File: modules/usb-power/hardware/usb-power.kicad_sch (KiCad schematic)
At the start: 0 parts

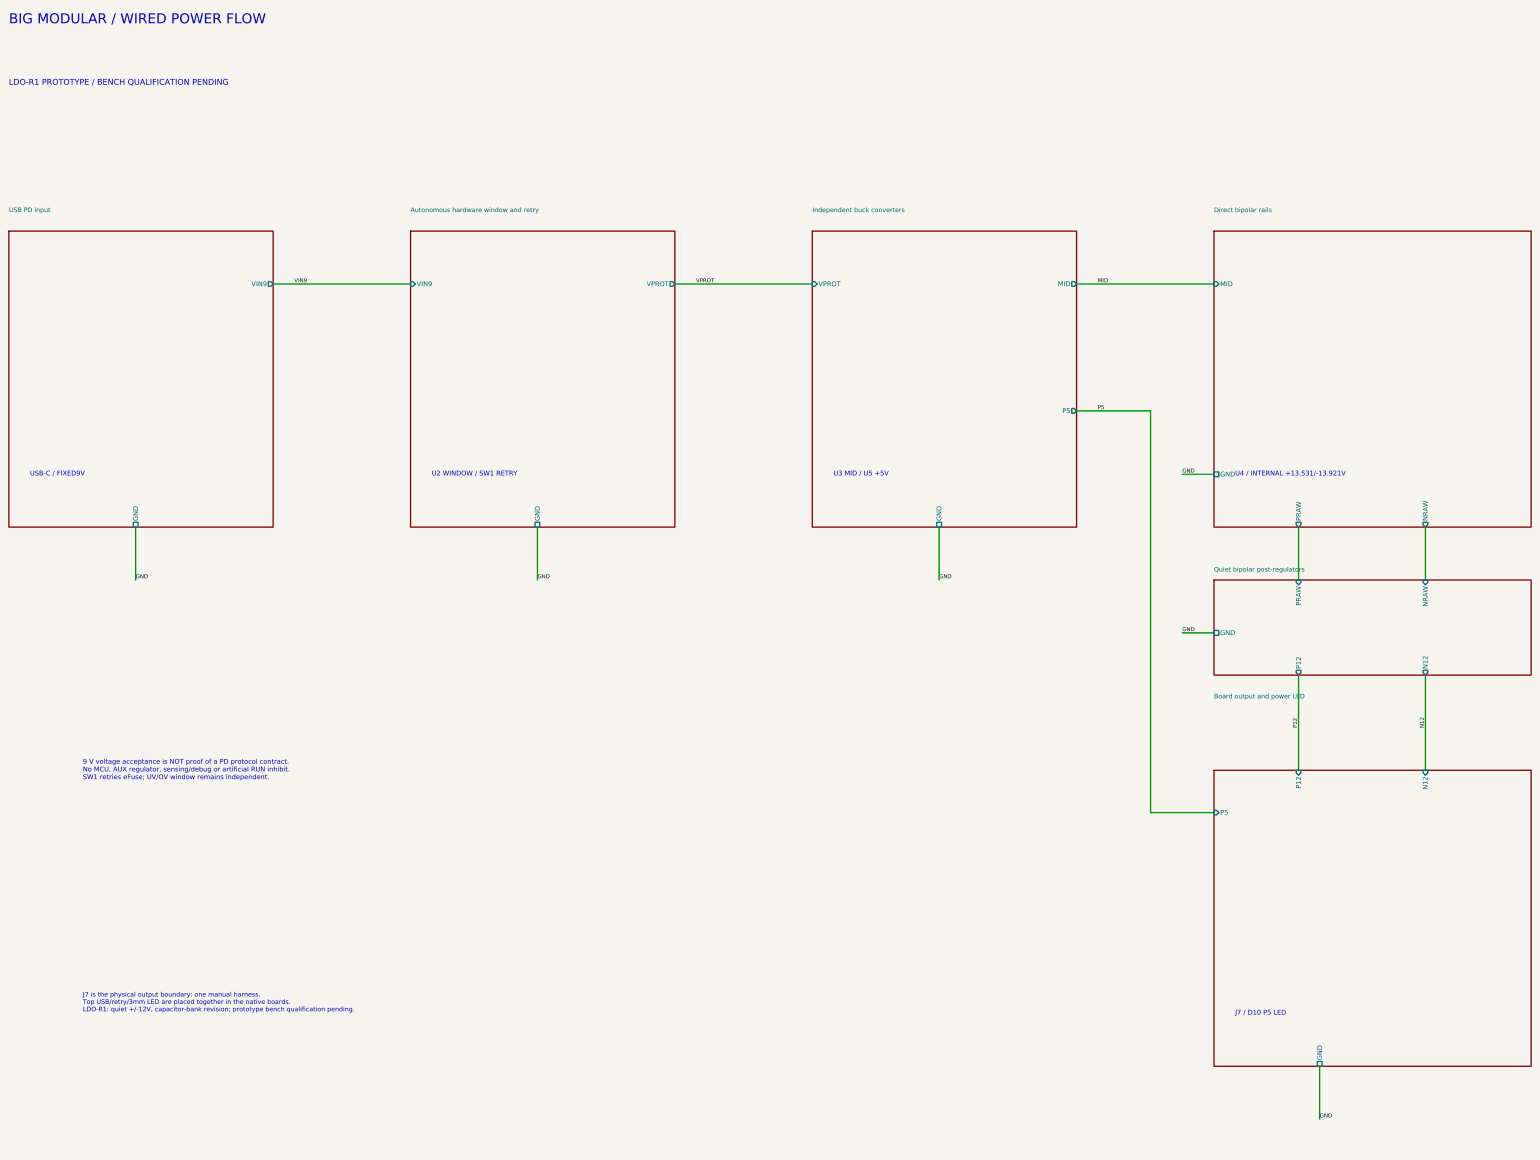
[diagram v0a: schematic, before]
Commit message: Save exact Astra SR2 schematic candidate and DeepSeek review; keep PCB unchanged
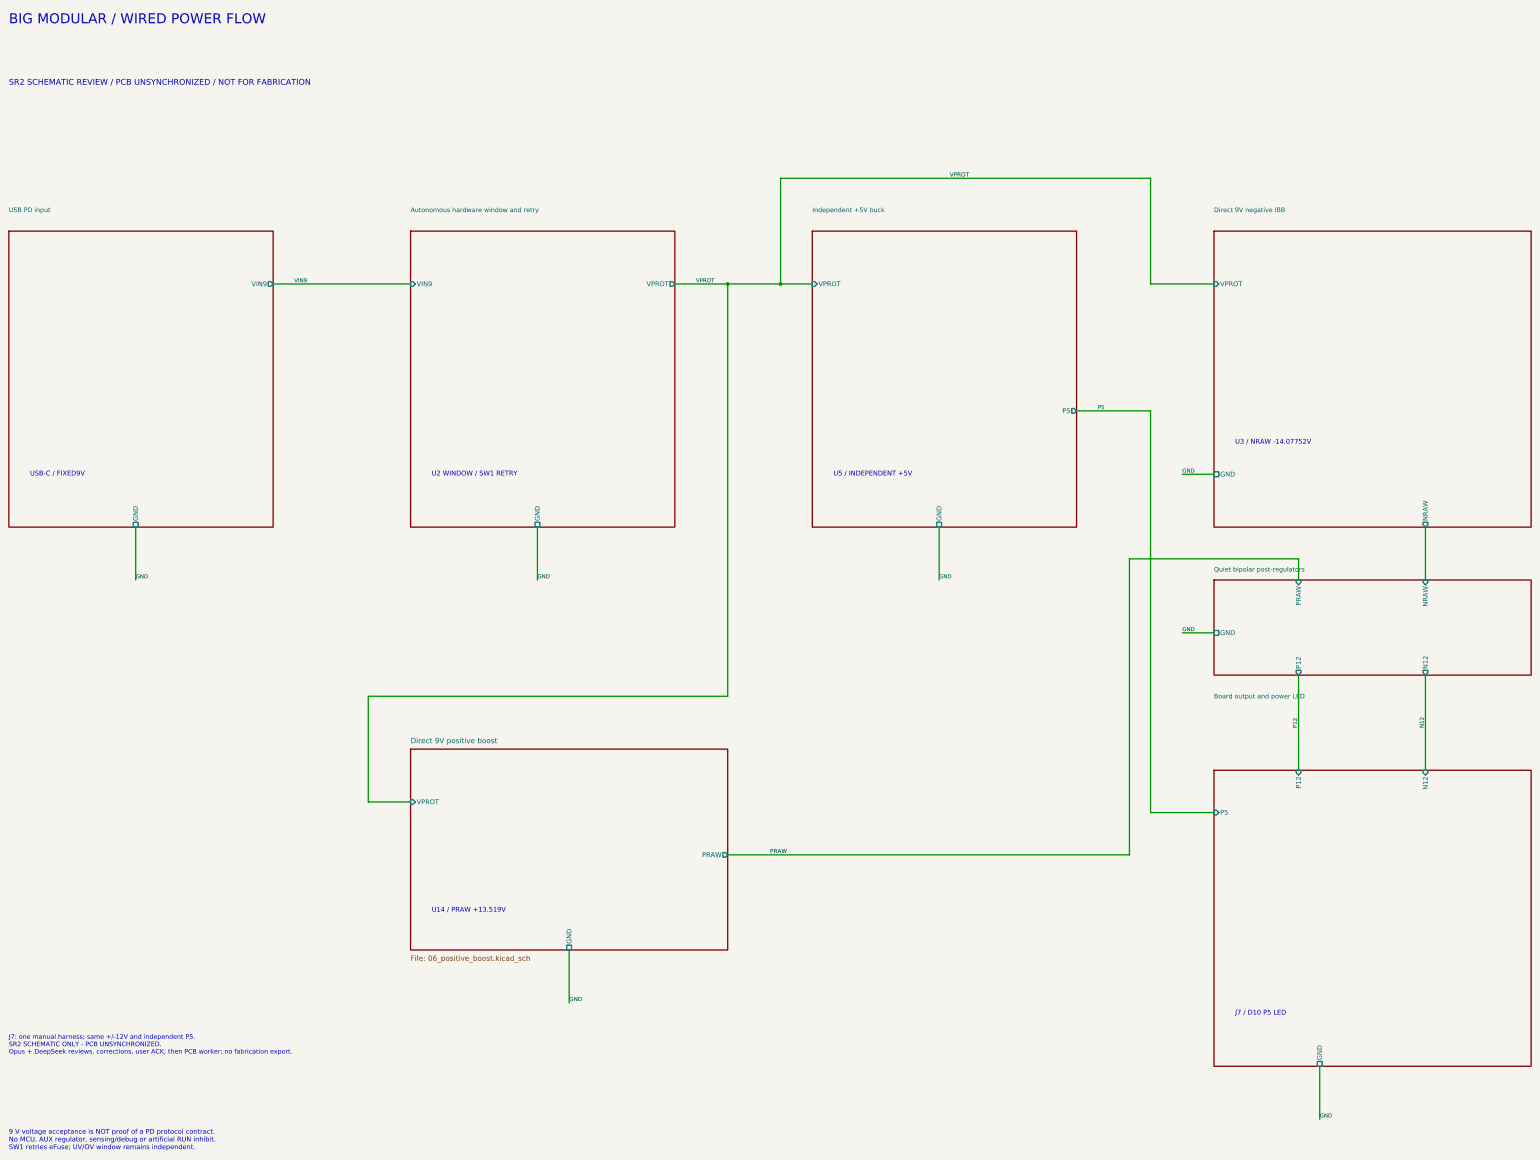
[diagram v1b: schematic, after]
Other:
- sheet Direct bipolar rails renamed Direct 9V negative IBB
- sheet Independent buck converters renamed Independent +5V buck
- added sheet Direct 9V positive boost (06_positive_boost.kicad_sch)
- sheet Direct 9V negative IBB ports: added VPROT; removed MID, PRAW
- sheet Independent +5V buck ports: added none; removed MID
- note added: "J7: one manual harness; same +/-12V and independent P5. SR2 SCHEMATIC ONLY - PCB UNSYNCHRONIZED. Opus + DeepSeek reviews, corrections, user ACK; then PCB worker; no fabrication export."
- note added: "SR2 SCHEMATIC REVIEW / PCB UNSYNCHRONIZED / NOT FOR FABRICATION"
- note added: "U14 / PRAW +13.519V"
- note added: "U3 / NRAW -14.07752V"
- note added: "U5 / INDEPENDENT +5V"
- note removed: "J7 is the physical output boundary: one manual harness. Top USB/retry/3mm LED are placed together in the native boards. LDO-R1: quiet +/-12V, capacitor-bank revision; prototype bench qualification pending."
- note removed: "LDO-R1 PROTOTYPE / BENCH QUALIFICATION PENDING"
- note removed: "U3 MID / U5 +5V"
- note removed: "U4 / INTERNAL +13.531/-13.921V"
